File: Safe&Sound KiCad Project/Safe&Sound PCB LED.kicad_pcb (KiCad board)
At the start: 2 copper layers, 37 parts, among them J1 USB_B_Micro, J2 Conn_01x02_Female, J3 Conn_01x03_Female, J4 Conn_01x03_Female, J5 Conn_01x05_Female, J6 Conn_01x07_Female, SW1 EN, SW2 MT, SW3 BOOT, SW4 BT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

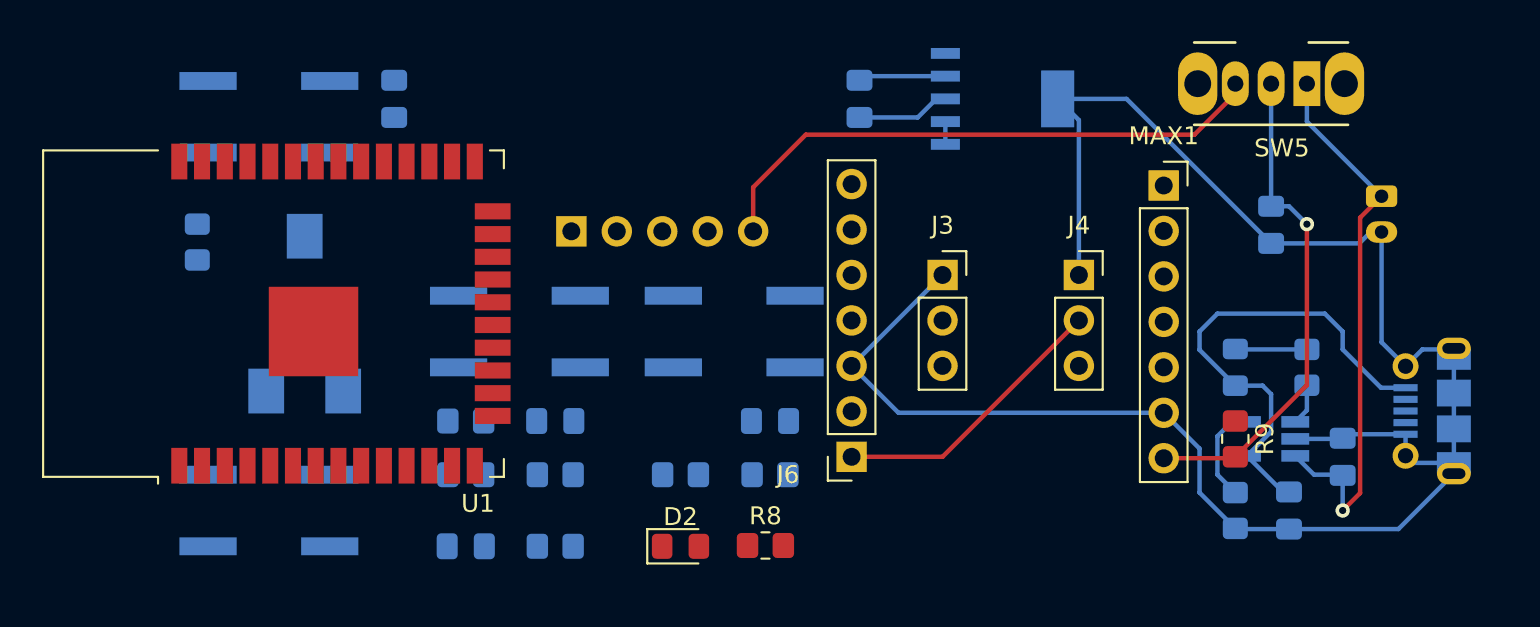
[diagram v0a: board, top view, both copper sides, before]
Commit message: PCB y archivos de fabricación
- Se agrega el LED de usuario
- Se trazan las rutas de la PCB
- Se generan los archivos de fabricación
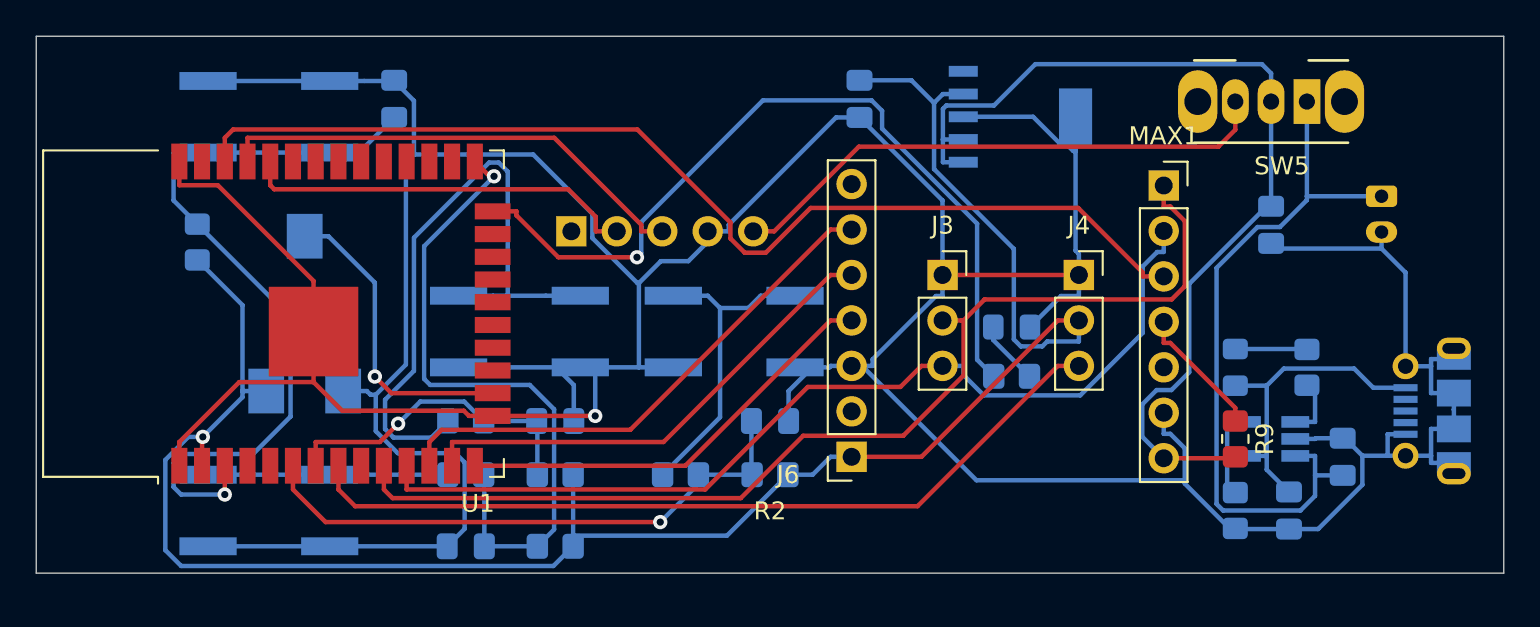
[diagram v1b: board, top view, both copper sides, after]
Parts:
- D2, R8: moved to B.Cu
- moved D2 22.2 mm to (160.5, 75.8), turned to 180 degrees
- moved R8 16.7 mm to (160.5, 78.5), turned to 180 degrees
- moved U2 1.41 mm to (161.0, 64.0)
- moved SW5 1.00 mm to (177.0, 63.1)
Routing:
- net GND: track 113.1 -> 288.3 mm, vias 0 -> 1
- net +3V3: track 20.8 -> 110.0 mm, vias 0 -> 1
- net LRC: track 0.00 -> 60.5 mm
- net D_AMP: track 0.00 -> 60.1 mm
- net BCLK: track 0.00 -> 54.1 mm
- net D_MIC: track 0.00 -> 46.3 mm
- net LED: track 0.00 -> 45.3 mm, vias 0 -> 1
- net Net-(C1-Pad2): track 0.00 -> 44.4 mm, vias 0 -> 1
- net Net-(C3-Pad1): track 0.00 -> 37.3 mm, vias 0 -> 1
- net Net-(R7-Pad2): track 0.00 -> 36.4 mm
- net MT: track 0.00 -> 32.1 mm, vias 0 -> 1
- net Xout: track 0.00 -> 29.8 mm
- net Yout: track 0.00 -> 27.5 mm
- net TXD0: track 0.00 -> 26.9 mm
- net VPP: track 29.7 -> 54.5 mm, vias 1 -> 0
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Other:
- board outline added: 82 x 30 mm

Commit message: PCB con zona GND y archivos de fabricación
- Se actualizan los archivos de fabricación de la PCB.
- Se aumentan distancias entre ciertas pistas para evitar problemas de tolerancia.
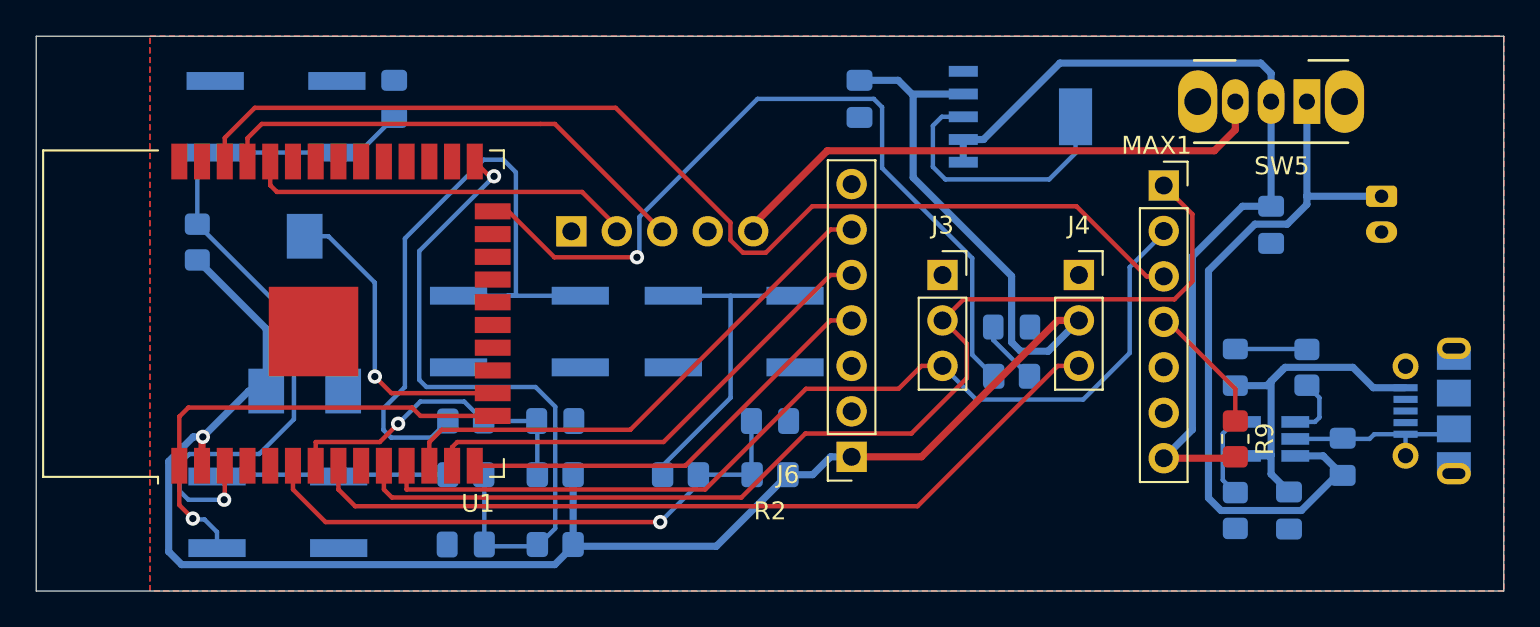
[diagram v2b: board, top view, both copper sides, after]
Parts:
- J1: value USB_B_Micro -> USB
- moved SW3 0.51 mm to (119.5, 86.1)
- moved SW1 0.40 mm to (119.4, 64.0)
- moved C3 0.10 mm to (130.0, 87.9)
- moved R4 0.10 mm to (135.0, 87.9)
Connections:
- SW5 pad : (no net) -> GND
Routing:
- net GND: track 288.3 -> 52.0 mm
- net VPP: track 54.5 -> 49.4 mm
- net Net-(C1-Pad2): track 44.4 -> 42.1 mm
- net Net-(R7-Pad2): track 36.4 -> 37.8 mm
- net +5V: track 17.9 -> 19.4 mm
- net LRC: track 60.5 -> 61.6 mm
- net D_AMP: track 60.1 -> 61.1 mm
- net +BATT: track 40.4 -> 41.4 mm
- net Net-(C3-Pad1): track 37.3 -> 37.9 mm
- added copper zone on B.Cu, net GND
- added copper zone on F.Cu, net GND
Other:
- board size 82 x 30 mm -> 82 x 31 mm
